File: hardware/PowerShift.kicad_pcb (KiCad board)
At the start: 2 copper layers, 54 parts, among them J10 SHIFT_OUT, J11 JST-ZR, J12 JST-ZR, J14 JST-ZR, J2 MICRO_USB, J3 JST-ZR, J4 JST-ZR, J5 SHIFT_IN, J6 SHIFT_IN, J7 AVR-PDI-6A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

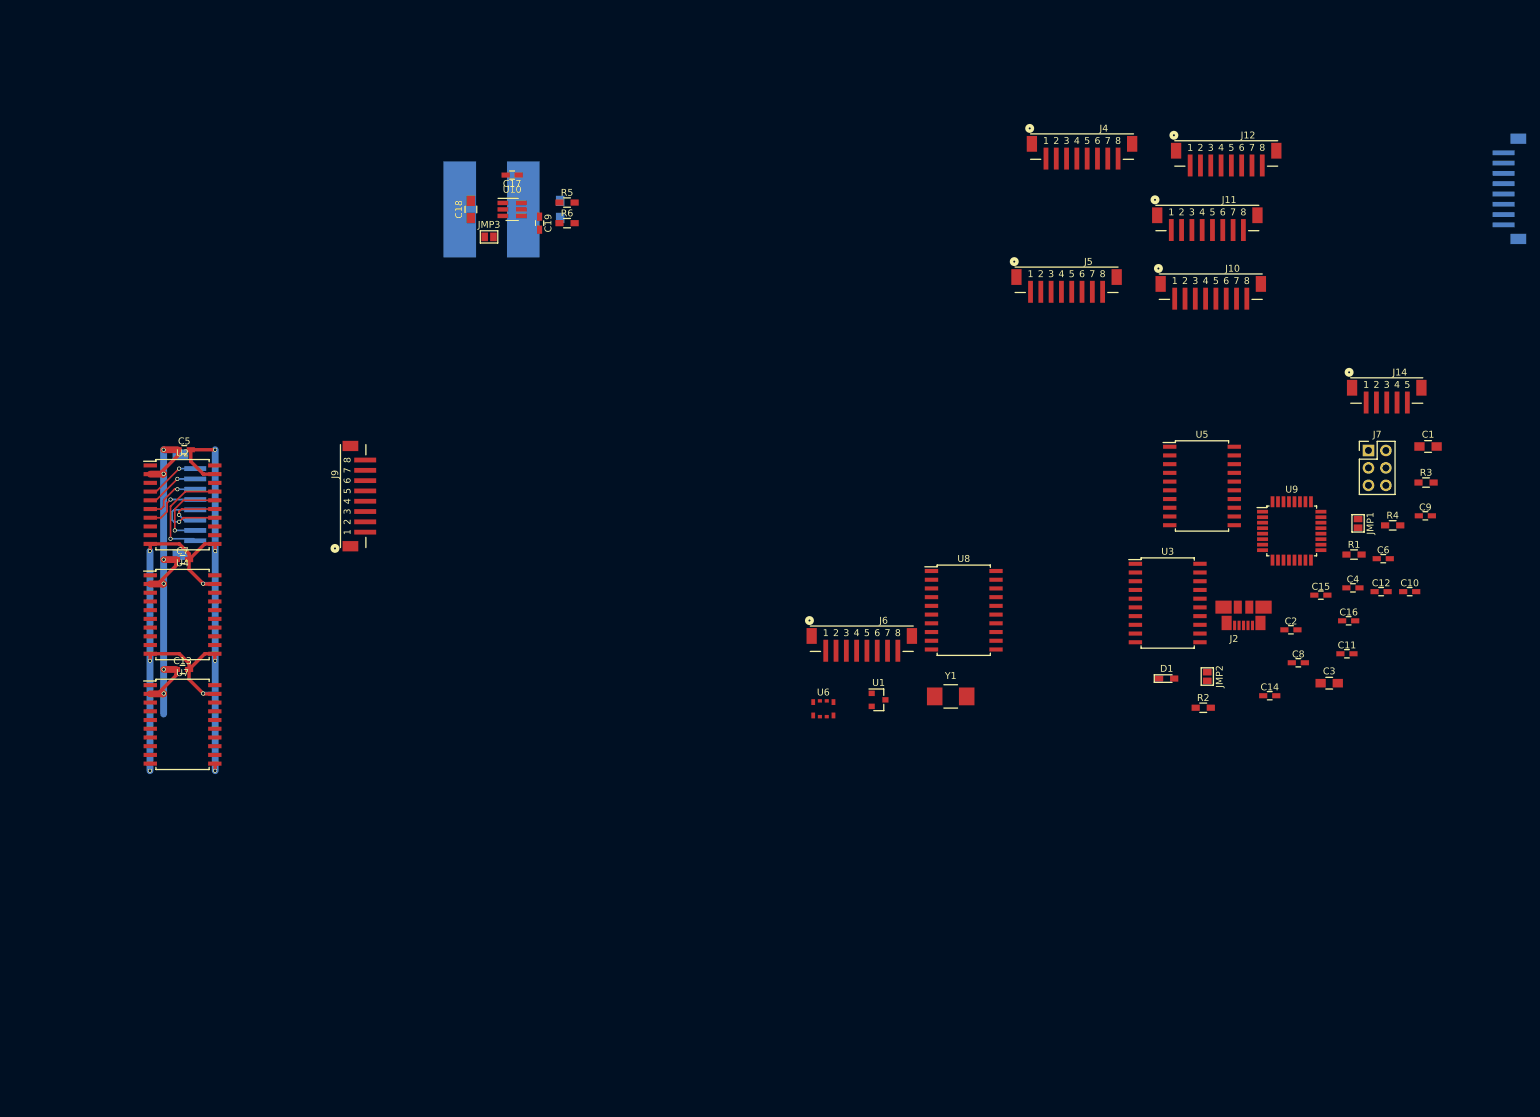
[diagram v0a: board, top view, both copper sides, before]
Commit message: Shift registers laid out
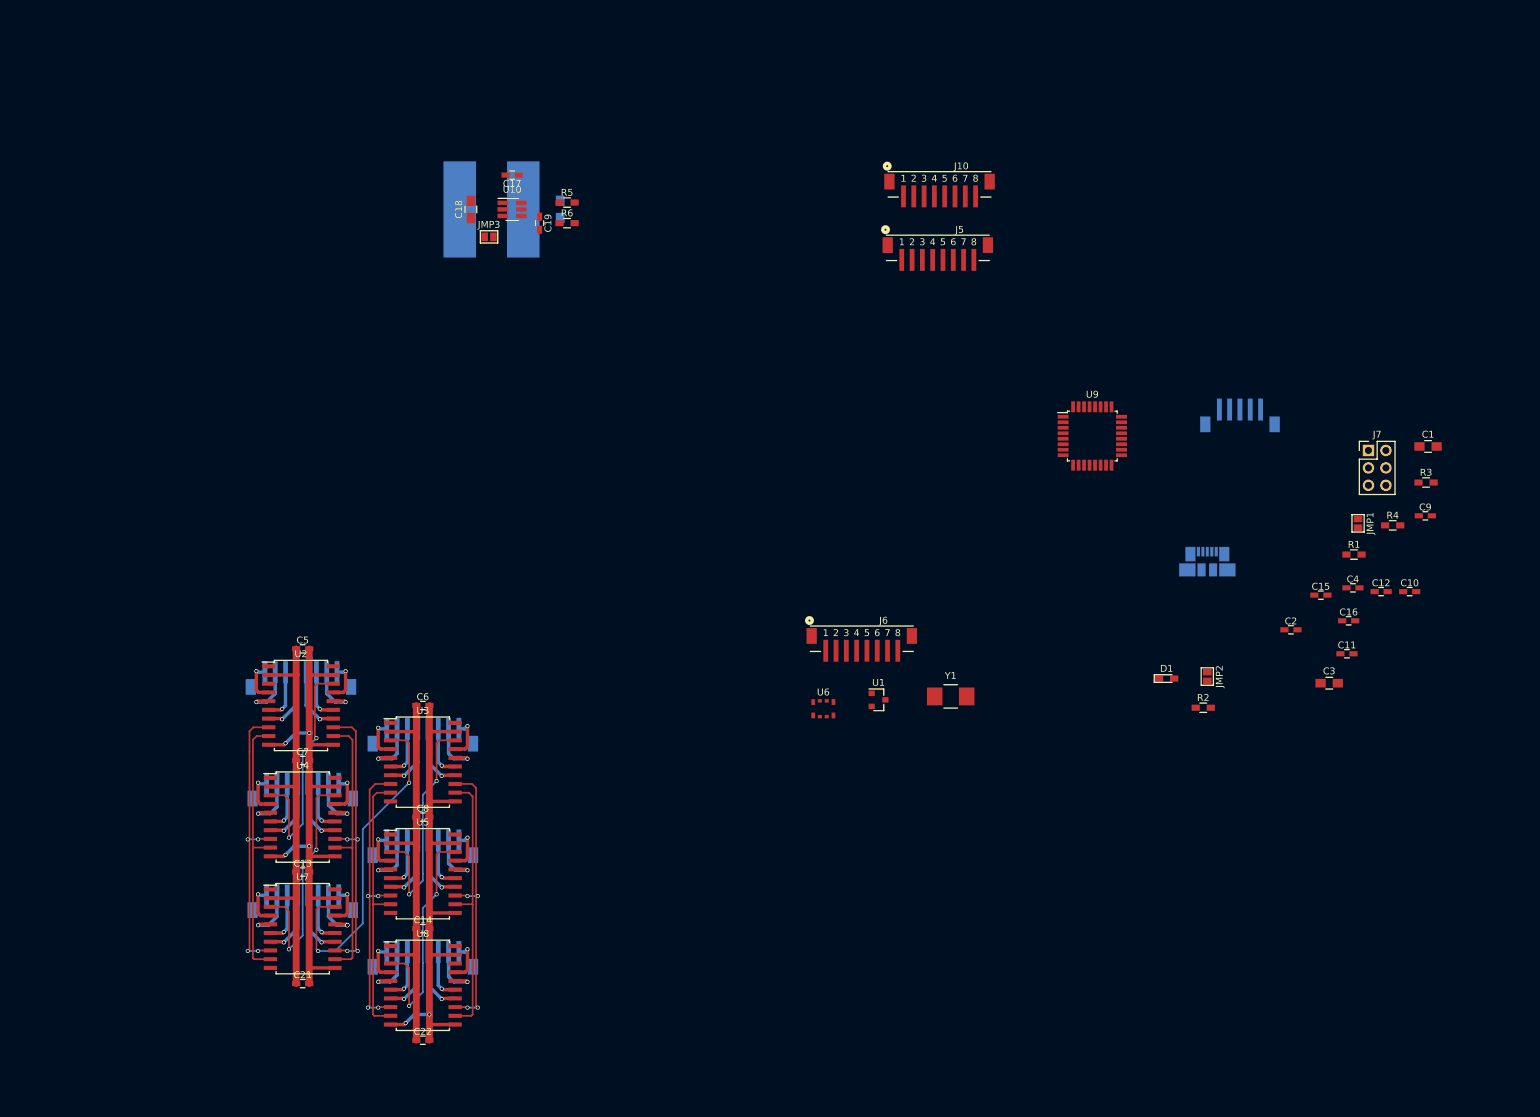
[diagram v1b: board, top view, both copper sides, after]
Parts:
- added C21: 100n, Capacitors_SMD:C_0603_HandSoldering, F.Cu at (77.5, 179.8)
- added C22: 100n, Capacitors_SMD:C_0603_HandSoldering, F.Cu at (95.0, 188.0)
- J11, J12, J14, J2, J4, J9: moved to B.Cu
- moved J8 197.3 mm to (77.5, 152.2), turned to 0 degrees
- moved J12 166.0 mm to (95.0, 176.8)
- moved J11 165.5 mm to (77.5, 168.5)
- moved C6 141.5 mm to (95.0, 139.2)
- moved C8 129.5 mm to (95.0, 155.5)
- moved J4 129.1 mm to (95.0, 144.2)
- moved C14 127.9 mm to (95.0, 171.8)
- moved U5 126.8 mm to (95.0, 163.8)
- moved U3 110.9 mm to (95.0, 147.5)
- moved U8 95.9 mm to (95.0, 180.0)
- moved J9 52.7 mm to (95.0, 160.5), turned to 0 degrees
- moved J10 42.2 mm to (170.2, 63.5)
- moved U7 34.5 mm to (77.5, 171.8)
- moved C13 34.3 mm to (77.5, 163.5)
- moved U4 34.3 mm to (77.5, 155.5)
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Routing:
- net /SRCK: track 0.00 -> 84.9 mm, vias 0 -> 8
- net /~SRCLR: track 0.00 -> 84.2 mm, vias 0 -> 8
- net /RCK: track 0.00 -> 79.7 mm
- net /~G: track 0.00 -> 79.2 mm
- net +3V3: track 67.5 -> 120.4 mm, vias 6 -> 0
- net Net-(U3-Pad3): track 0.00 -> 49.1 mm, vias 0 -> 2
- net Net-(U2-Pad18): track 0.00 -> 35.1 mm, vias 0 -> 2
- net Net-(U5-Pad18): track 0.00 -> 35.0 mm, vias 0 -> 2
- net Net-(U4-Pad18): track 0.00 -> 35.0 mm, vias 0 -> 2
- net Net-(U3-Pad18): track 0.00 -> 35.0 mm, vias 0 -> 2
- net GND: track 132.9 -> 161.4 mm, vias 9 -> 6
- net Net-(J3-Pad8): track 15.8 -> 6.02 mm
- net Net-(J9-Pad5): track 0.00 -> 9.67 mm, vias 0 -> 1
- net Net-(J9-Pad4): track 0.00 -> 9.67 mm, vias 0 -> 1
- net Net-(J8-Pad5): track 0.00 -> 9.67 mm, vias 0 -> 1
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
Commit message: MCU planning
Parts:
- J7: footprint Pin_Headers:Pin_Header_Straight_2x03_Pitch2.54mm -> kuro:3x2_1.27mm_SMD_header; moved to B.Cu
- JMP1: moved to B.Cu
- moved J10 156.0 mm to (62.1, 176.0), turned to 90 degrees
- moved J5 127.3 mm to (62.5, 141.0), turned to 270 degrees
- moved JMP2 84.6 mm to (158.0, 67.8)
- moved R1 70.6 mm to (162.6, 136.2)
- moved U6 64.1 mm to (206.2, 103.5), turned to 180 degrees
- moved C10 60.0 mm to (186.2, 93.5), turned to 180 degrees
- moved C12 59.8 mm to (179.8, 98.7), turned to 270 degrees
- moved R3 58.9 mm to (182.8, 98.8), turned to 270 degrees
- moved J7 54.4 mm to (178.5, 106.8)
- moved C1 52.8 mm to (194.5, 125.8), turned to 180 degrees
- moved JMP1 51.8 mm to (185.5, 88.2), turned to 180 degrees
- moved R2 51.2 mm to (157.5, 137.2)
- moved Y1 46.2 mm to (200.0, 101.2), turned to 270 degrees
- moved D1 44.4 mm to (200.0, 91.0)
- moved R4 43.8 mm to (200.2, 88.0)
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
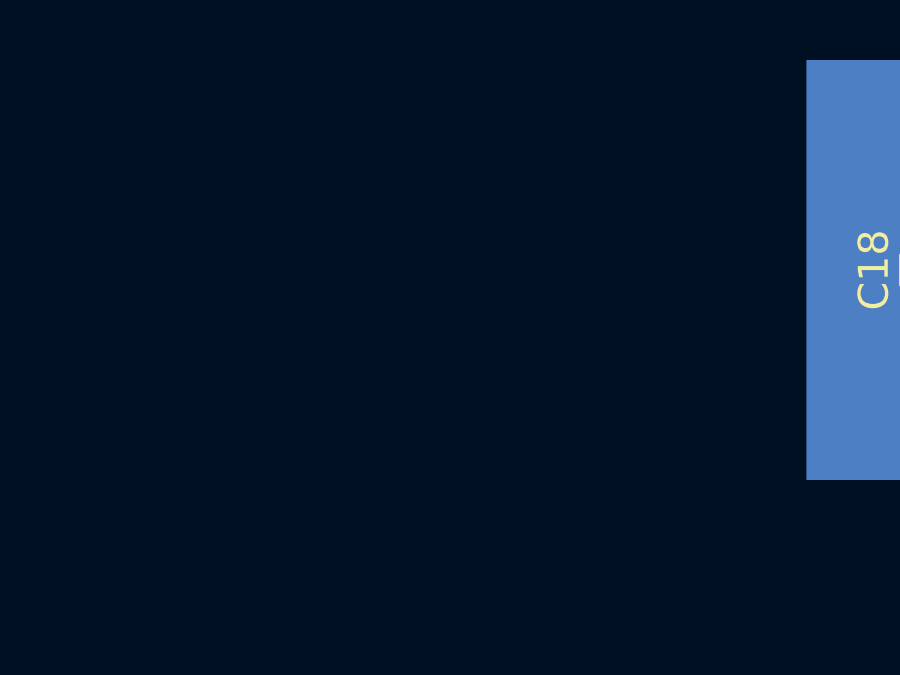
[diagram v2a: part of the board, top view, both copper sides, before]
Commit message: DC jack footprint
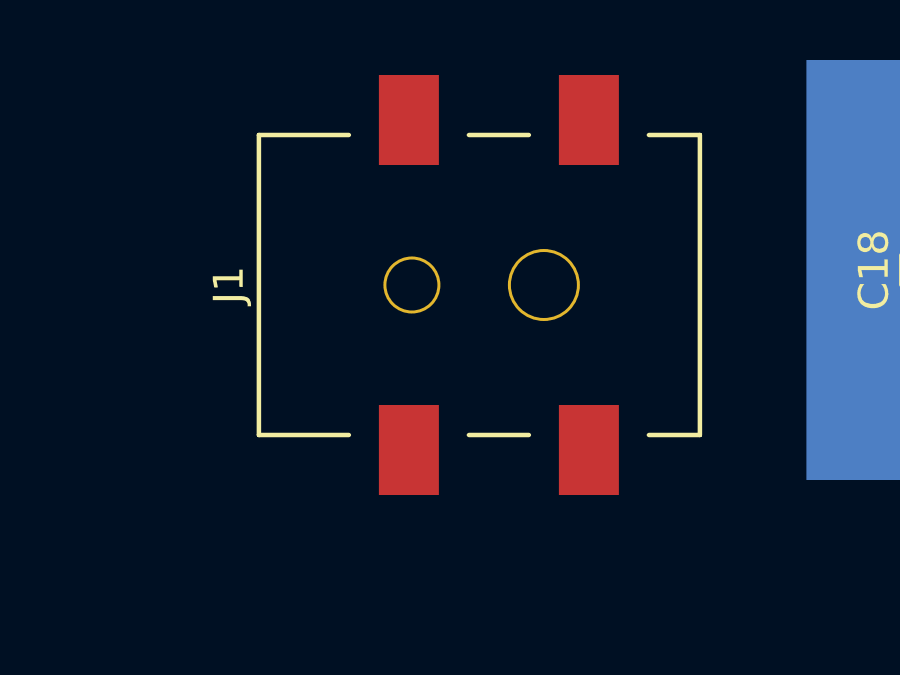
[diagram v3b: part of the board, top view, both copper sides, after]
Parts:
- added J1: Barrel_Jack, kuro:DC_Jack_SMD_FC6814xS_6941, F.Cu at (79.8, 67.5)
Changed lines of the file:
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@@
 (kicad_pcb (version 4) (host pcbnew 4.0.7)
   (general
-    (links 217)
-    (no_connects 115)
+    (links 221)
+    (no_connects 119)
     (area 0 0 0 0)
     (thickness 1.6)
@@
     (tracks 522)
     (zones 0)
-    (modules 56)
+    (modules 57)
     (nets 86)
   )
@@
       (net 2 GND))
   )
+  (module kuro:DC_Jack_SMD_FC6814xS_6941 (layer F.Cu)
+    (at 79.75 67.5 90)
+    (descr http://www.farnell.com/datasheets/1864271.pdf)
+    (fp_text reference J1 (at 0 -1 90) (layer F.SilkS)
+      (effects (font (size 1 1) (thickness 0.15)))
+    )
+    (fp_text value Barrel_Jack (at 0 16 90) (layer F.Fab) hide
+      (effects (font (size 1 1) (thickness 0.15)))
+    )
+    (fp_line (start 8 -10) (end -8 -10) (layer F.CrtYd) (width 0.15))
+    (fp_line (start 8 16) (end 8 -10) (layer F.CrtYd) (width 0.15))
+    (fp_line (start -8 16) (end 8 16) (layer F.CrtYd) (width 0.15))
+    (fp_line (start -8 -10) (end -8 16) (layer F.CrtYd) (width 0.15))
+    (fp_line (start -5 13) (end -5 14.7) (layer F.SilkS) (width 0.15))
+    (fp_line (start 5 13) (end 5 14.7) (layer F.SilkS) (width 0.15))
+    (fp_line (start -5 14.7) (end 5 14.7) (layer F.SilkS) (width 0.15))
+    (fp_line (start 5 7) (end 5 9) (layer F.SilkS) (width 0.15))
+    (fp_line (start -5 7) (end -5 9) (layer F.SilkS) (width 0.15))
+    (fp_line (start -5 0) (end -5 3) (layer F.SilkS) (width 0.15))
+    (fp_line (start 5 0) (end 5 3) (layer F.SilkS) (width 0.15))
+    (fp_line (start -5 0) (end 5 0) (layer F.SilkS) (width 0.15))
+    (pad 1 smd rect (at -5.5 11 90) (size 3 2) (layers F.Cu F.Paste F.Mask)
+      (net 9 "Net-(C18-Pad1)"))
+    (pad 1 smd rect (at -5.5 5 90) (size 3 2) (layers F.Cu F.Paste F.Mask)
+      (net 9 "Net-(C18-Pad1)"))
+    (pad 3 smd rect (at 5.5 5 90) (size 3 2) (layers F.Cu F.Paste F.Mask)
+      (net 2 GND))
+    (pad 2 smd rect (at 5.5 11 90) (size 3 2) (layers F.Cu F.Paste F.Mask)
+      (net 2 GND))
+    (pad "" np_thru_hole circle (at 0 5.1 90) (size 1.9 1.9) (drill 1.7) (layers *.Cu *.Mask))
+    (pad "" np_thru_hole circle (at 0 9.5 90) (size 2.4 2.4) (drill 2.2) (layers *.Cu *.Mask))
+  )
   (segment (start 95.95 185.75) (end 95.95 184.25) (width 1) (layer F.Cu) (net 2))

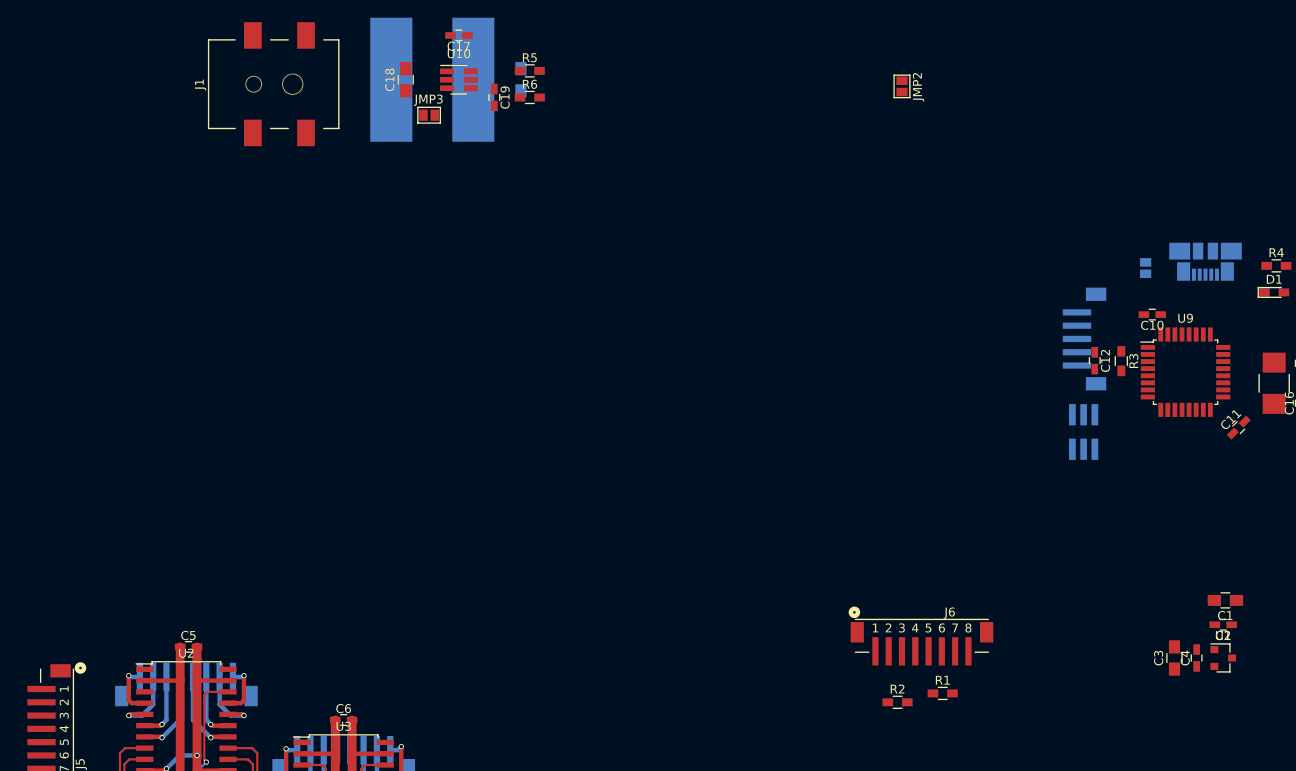
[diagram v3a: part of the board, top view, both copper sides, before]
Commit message: Power supply layout
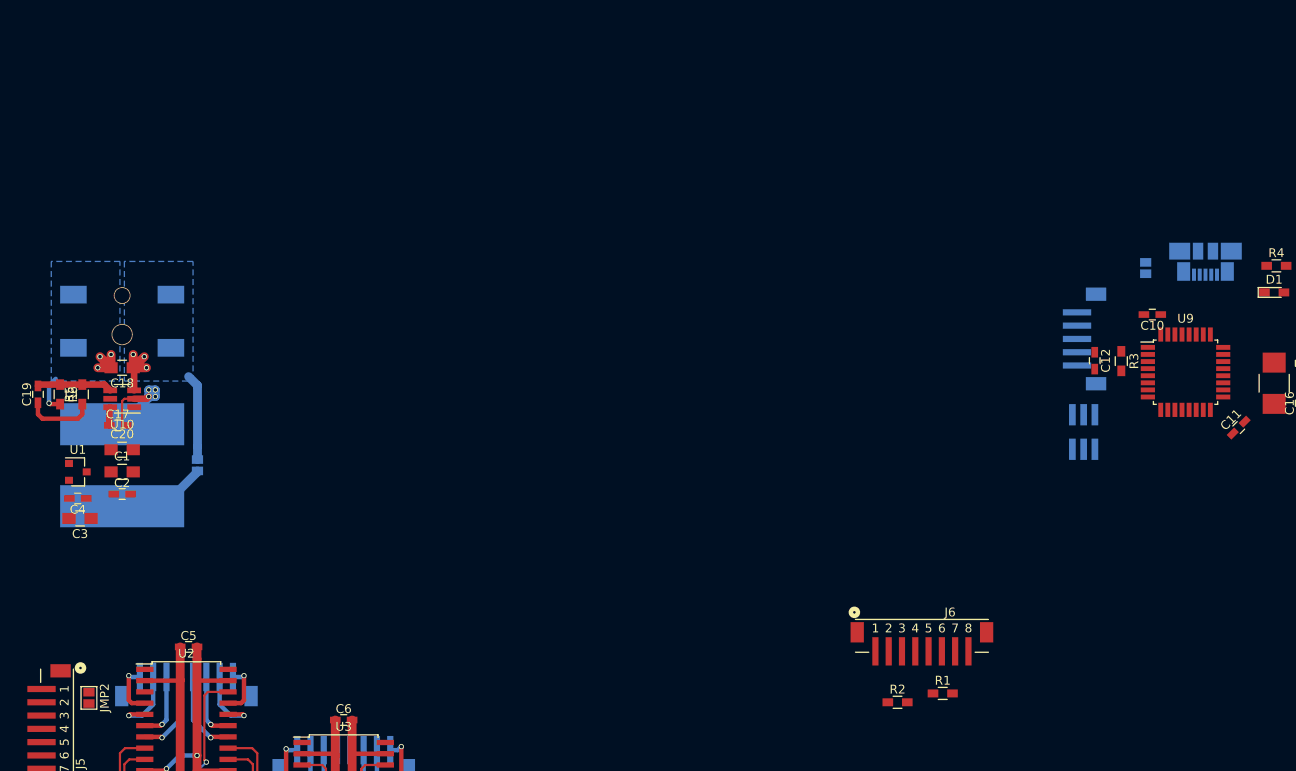
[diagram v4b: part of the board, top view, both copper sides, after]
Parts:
- C20: moved to F.Cu
- J1, JMP3: moved to B.Cu
- moved U1 130.9 mm to (65.0, 111.2)
- moved C4 127.5 mm to (65.0, 114.2), turned to 180 degrees
- moved C1 125.3 mm to (70.0, 111.2), turned to 0 degrees
- moved C2 125.1 mm to (70.0, 113.8), turned to 0 degrees
- moved C3 124.5 mm to (65.2, 116.5), turned to 180 degrees
- moved JMP2 114.8 mm to (66.2, 136.8)
- moved R6 62.7 mm to (63.0, 102.5), turned to 270 degrees
- moved R5 62.3 mm to (65.5, 102.5), turned to 90 degrees
- moved C19 61.4 mm to (60.5, 102.5), turned to 90 degrees
- moved C20 61.4 mm to (70.0, 108.8), turned to 0 degrees
- moved C17 58.5 mm to (69.5, 106.0), turned to 0 degrees
- moved L1 55.8 mm to (70.0, 110.5), turned to 0 degrees
- moved U10 52.3 mm to (70.0, 103.0), turned to 180 degrees
- moved JMP3 47.4 mm to (78.5, 110.5), turned to 180 degrees
- moved C18 45.6 mm to (70.0, 99.5), turned to 180 degrees
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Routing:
- net VPP: track 0.00 -> 18.1 mm
- net Net-(C18-Pad1): track 0.00 -> 17.1 mm, vias 0 -> 3
- net Net-(C17-Pad2): track 0.00 -> 13.5 mm, vias 0 -> 4
- net GND: track 161.4 -> 170.5 mm, vias 6 -> 10
- net Net-(C19-Pad2): track 0.00 -> 8.48 mm
- net Net-(C17-Pad1): track 0.00 -> 2.09 mm
- added copper zone on B.Cu, net GND
- added copper zone on B.Cu, net Net-(C18-Pad1)

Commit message: Aligned drivers
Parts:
- added JMP4: GS3, Connectors:GS3, F.Cu at (127.2, 57.8)
- added M1: TEST, Mounting_Holes:MountingHole_2.7mm_M2.5_Pad, F.Cu at (55.0, 90.0)
- added M2: TEST, Mounting_Holes:MountingHole_2.7mm_M2.5_Pad, F.Cu at (104.5, 88.8)
- added M3: TEST, Mounting_Holes:MountingHole_2.7mm_M2.5_Pad, F.Cu at (112.8, 194.5)
- added M4: TEST, Mounting_Holes:MountingHole_2.7mm_M2.5_Pad, F.Cu at (65.2, 193.0)
- J10: value SHIFT_OUT -> SHIFT_IN
- J5: footprint kuro:B8B-ZR-SM4-TF -> Pin_Headers:Pin_Header_Straight_1x08_Pitch2.54mm
- moved J10 77.7 mm to (39.2, 101.8)
- moved J5 18.1 mm to (63.5, 159.1), turned to 0 degrees
- moved C14 8.25 mm to (95.0, 163.5)
- moved C22 8.25 mm to (95.0, 179.8)
- moved C6 8.25 mm to (95.0, 131.0)
- moved C8 8.25 mm to (95.0, 147.2)
- moved J12 8.25 mm to (95.0, 168.5)
- moved J4 8.25 mm to (95.0, 136.0)
- moved J9 8.25 mm to (95.0, 152.2)
- moved U3 8.25 mm to (95.0, 139.2)
- moved U5 8.25 mm to (95.0, 155.5)
- moved U8 8.25 mm to (95.0, 171.8)
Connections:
- J10 pad 2: +3V3 -> VPP
- J10 pad 3: GND -> VPP
- J10 pad 4: /SRCK -> VPP
- J10 pad 5: /RCK -> VPP
- J10 pad 6: /~G -> VPP
- J10 pad 7: /~SRCLR -> VPP
- J10 pad 8: /SER_OUT -> VPP
- J5 pad 8: /SER_IN -> Net-(J5-Pad8)
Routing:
- net Net-(U3-Pad3): track 49.1 -> 57.3 mm

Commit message: Board outline
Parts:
- J6, R1, R2: moved to B.Cu
- moved JMP4 101.8 mm to (55.5, 130.0), turned to 180 degrees
- moved R2 77.7 mm to (219.0, 89.8), turned to 270 degrees
- moved R1 75.7 mm to (218.0, 84.7), turned to 270 degrees
- moved J6 67.0 mm to (211.7, 87.0), turned to 270 degrees
- moved M3 60.9 mm to (96.0, 136.0)
- moved M4 58.1 mm to (54.0, 136.0)
- moved C1 49.0 mm to (72.0, 62.2)
- moved C17 49.0 mm to (71.5, 57.0)
- moved C18 49.0 mm to (72.0, 50.5)
- moved C19 49.0 mm to (62.5, 53.5)
- moved C2 49.0 mm to (72.0, 64.8)
- moved C20 49.0 mm to (72.0, 59.8)
- moved C3 49.0 mm to (67.2, 67.5)
- moved C4 49.0 mm to (67.0, 65.2)
- moved J1 49.0 mm to (72.0, 37.2)
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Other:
- board outline added: 50 x 100 mm
